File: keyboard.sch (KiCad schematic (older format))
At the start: 8 parts, among them SW3 MENY, SW4 LEFT, SW5 UP, SW6 ENTER, SW7 DOWN, SW8 RETURN, SW9 RIGHT

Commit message: Добавил LCD. Уже есть набросок формата платы с экраном и кнопками.
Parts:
- SW3, SW4, SW5, SW6, SW7, SW8, SW9: footprint Button_Switch_THT:SW_PUSH_6mm_H13mm -> button:SW_PUSH_6x6x13
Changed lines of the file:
@@
 $Descr A4 11693 8268
 encoding utf-8
-Sheet 8 9
+Sheet 8 11
 Title ""
 Date ""
@@
 F 0 "SW3" H 4300 3285 50  0000 C CNN
 F 1 "MENY" H 4300 3194 50  0000 C CNN
-F 2 "Button_Switch_THT:SW_PUSH_6mm_H13mm" H 4300 3200 50  0001 C CNN
+F 2 "button:SW_PUSH_6x6x13" H 4300 3200 50  0001 C CNN
 F 3 "~" H 4300 3200 50  0001 C CNN
 	1    4300 3000
@@
 F 0 "SW5" H 4900 3285 50  0000 C CNN
 F 1 "UP" H 4900 3194 50  0000 C CNN
-F 2 "Button_Switch_THT:SW_PUSH_6mm_H13mm" H 4900 3200 50  0001 C CNN
+F 2 "button:SW_PUSH_6x6x13" H 4900 3200 50  0001 C CNN
 F 3 "~" H 4900 3200 50  0001 C CNN
 	1    4900 3000
@@
 F 0 "SW8" H 5500 3285 50  0000 C CNN
 F 1 "RETURN" H 5500 3194 50  0000 C CNN
-F 2 "Button_Switch_THT:SW_PUSH_6mm_H13mm" H 5500 3200 50  0001 C CNN
+F 2 "button:SW_PUSH_6x6x13" H 5500 3200 50  0001 C CNN
 F 3 "~" H 5500 3200 50  0001 C CNN
 	1    5500 3000
@@
 F 0 "SW4" H 4300 3785 50  0000 C CNN
 F 1 "LEFT" H 4300 3694 50  0000 C CNN
-F 2 "Button_Switch_THT:SW_PUSH_6mm_H13mm" H 4300 3700 50  0001 C CNN
+F 2 "button:SW_PUSH_6x6x13" H 4300 3700 50  0001 C CNN
 F 3 "~" H 4300 3700 50  0001 C CNN
 	1    4300 3500
@@
 F 0 "SW6" H 4900 3785 50  0000 C CNN
 F 1 "ENTER" H 4900 3694 50  0000 C CNN
-F 2 "Button_Switch_THT:SW_PUSH_6mm_H13mm" H 4900 3700 50  0001 C CNN
+F 2 "button:SW_PUSH_6x6x13" H 4900 3700 50  0001 C CNN
 F 3 "~" H 4900 3700 50  0001 C CNN
 	1    4900 3500
@@
 F 0 "SW9" H 5500 3785 50  0000 C CNN
 F 1 "RIGHT" H 5500 3694 50  0000 C CNN
-F 2 "Button_Switch_THT:SW_PUSH_6mm_H13mm" H 5500 3700 50  0001 C CNN
+F 2 "button:SW_PUSH_6x6x13" H 5500 3700 50  0001 C CNN
 F 3 "~" H 5500 3700 50  0001 C CNN
 	1    5500 3500
@@
 F 0 "SW7" H 4900 4285 50  0000 C CNN
 F 1 "DOWN" H 4900 4194 50  0000 C CNN
-F 2 "Button_Switch_THT:SW_PUSH_6mm_H13mm" H 4900 4200 50  0001 C CNN
+F 2 "button:SW_PUSH_6x6x13" H 4900 4200 50  0001 C CNN
 F 3 "~" H 4900 4200 50  0001 C CNN
 	1    4900 4000

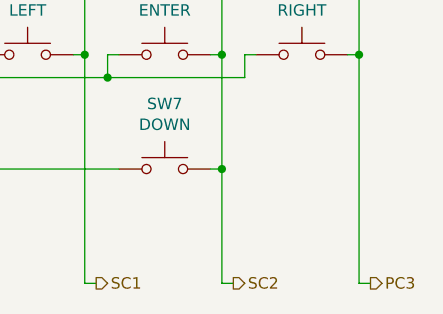
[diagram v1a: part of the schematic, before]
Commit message: dcdc доделан на 5V.
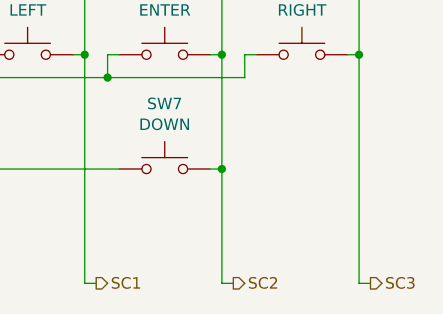
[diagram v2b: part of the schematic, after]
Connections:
- net PC3 renamed SC3
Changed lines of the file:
@@
 SC2
 Text HLabel 5800 4500 2    50   Output ~ 0
-PC3
+SC3
 Wire Wire Line
 	4550 3500 4550 4500
